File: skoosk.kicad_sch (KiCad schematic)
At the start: 90 parts, among them SW1 SW_Push, U1 ProMicro

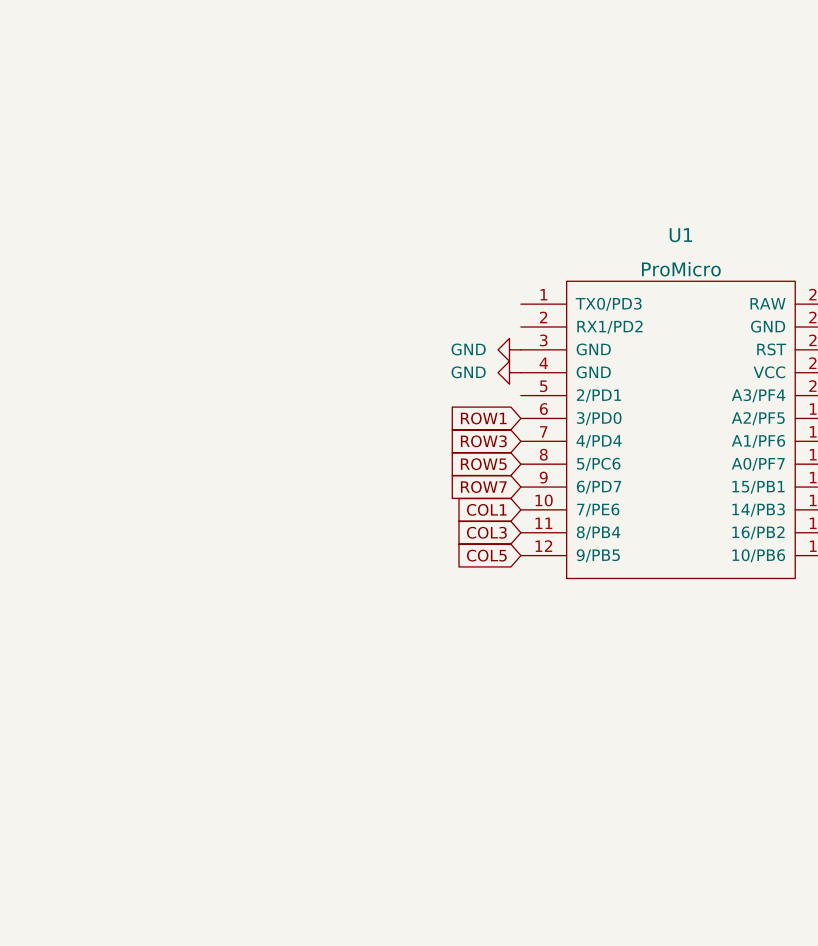
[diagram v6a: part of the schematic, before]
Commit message: GND filling done, added some ideas
maybe a rotary encoder and rgd leds?
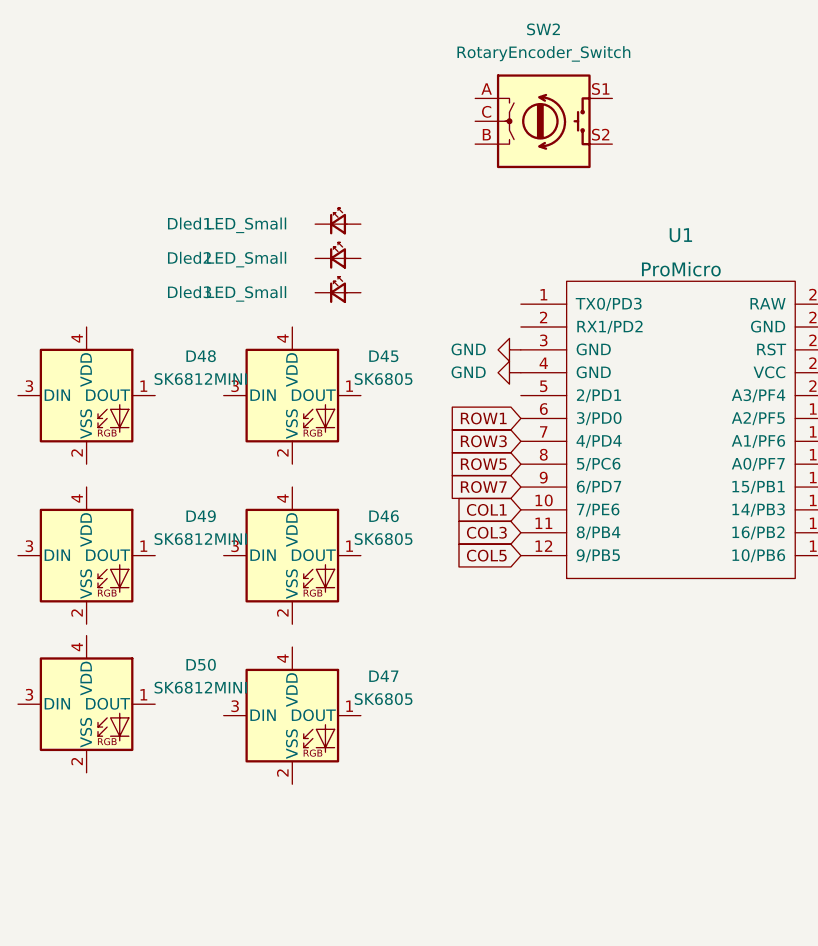
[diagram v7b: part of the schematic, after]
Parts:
- added D45, D46, D47: SK6805, LED_SMD:LED_SK6805_PLCC4_2.4x2.7mm_P1.3mm, symbol LED:SK6805
- added D48, D49, D50: SK6812MINI, LED_SMD:LED_SK6812MINI_PLCC4_3.5x3.5mm_P1.75mm, symbol LED:SK6812MINI
- added Dled1, Dled2, Dled3: LED_Small, LED_THT:LED_D5.0mm_Clear, symbol Device:LED_Small
- added SW2: RotaryEncoder_Switch, Keebio-Parts:RotaryEncoder_Alps_EC11E-Switch_Vertical_H20mm, symbol Device:RotaryEncoder_Switch
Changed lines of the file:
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@@
     (pin "2")
+  )
+  (symbol (lib_id "LED:SK6812MINI") (at -2.54 78.74 0) (unit 1)
+    (in_bom yes) (on_board yes) (fields_autoplaced)
+    (property "Reference" "D48" (id 0) (at 10.16 74.4093 0))
+    (property "Value" "SK6812MINI" (id 1) (at 10.16 76.9493 0))
+    (property "Footprint" "LED_SMD:LED_SK6812MINI_PLCC4_3.5x3.5mm_P1.75mm" (id 2) (at -1.27 86.36 0)
+      (effects (font (size 1.27 1.27)) (justify left top) hide)
+    )
+    (property "Datasheet" "https://cdn-shop.adafruit.com/product-files/2686/SK6812MINI_REV.01-1-2.pdf" (id 3) (at 0 88.265 0)
+      (effects (font (size 1.27 1.27)) (justify left top) hide)
+    )
+    (pin "1")
+    (pin "2")
+    (pin "3")
+    (pin "4")
   )
   (symbol (lib_id "MX_Alps_Hybrid:MX-NoLED") (at 154.94 92.71 0) (unit 1)
@@
     (pin "2")
   )
+  (symbol (lib_id "Device:LED_Small") (at 25.4 63.5 0) (unit 1)
+    (in_bom yes) (on_board yes)
+    (property "Reference" "Dled2" (id 0) (at 8.89 63.5 0))
+    (property "Value" "LED_Small" (id 1) (at 15.24 63.5 0))
+    (property "Footprint" "LED_THT:LED_D5.0mm_Clear" (id 2) (at 25.4 63.5 90)
+      (effects (font (size 1.27 1.27)) hide)
+    )
+    (property "Datasheet" "~" (id 3) (at 25.4 63.5 90)
+      (effects (font (size 1.27 1.27)) hide)
+    )
+    (pin "1")
+    (pin "2")
+  )
   (symbol (lib_id "MX_Alps_Hybrid:MX-NoLED") (at 256.54 74.93 0) (unit 1)
     (in_bom yes) (on_board yes) (fields_autoplaced)
@@
     (pin "2")
   )
+  (symbol (lib_id "LED:SK6805") (at 20.32 114.3 0) (unit 1)
+    (in_bom yes) (on_board yes) (fields_autoplaced)
+    (property "Reference" "D47" (id 0) (at 30.48 109.9693 0))
+    (property "Value" "SK6805" (id 1) (at 30.48 112.5093 0))
+    (property "Footprint" "LED_SMD:LED_SK6805_PLCC4_2.4x2.7mm_P1.3mm" (id 2) (at 21.59 121.92 0)
+      (effects (font (size 1.27 1.27)) (justify left top) hide)
+    )
+    (property "Datasheet" "https://cdn-shop.adafruit.com/product-files/3484/3484_Datasheet.pdf" (id 3) (at 22.86 123.825 0)
+      (effects (font (size 1.27 1.27)) (justify left top) hide)
+    )
+    (pin "1")
+    (pin "2")
+    (pin "3")
+    (pin "4")
+  )
   (symbol (lib_id "Device:D_Small") (at 204.47 81.28 90) (unit 1)
     (in_bom yes) (on_board yes) (fields_autoplaced)
@@
     (pin "2")
   )
+  (symbol (lib_id "LED:SK6805") (at 20.32 96.52 0) (unit 1)
+    (in_bom yes) (on_board yes) (fields_autoplaced)
+    (property "Reference" "D46" (id 0) (at 30.48 92.1893 0))
+    (property "Value" "SK6805" (id 1) (at 30.48 94.7293 0))
+    (property "Footprint" "LED_SMD:LED_SK6805_PLCC4_2.4x2.7mm_P1.3mm" (id 2) (at 21.59 104.14 0)
+      (effects (font (size 1.27 1.27)) (justify left top) hide)
+    )
+    (property "Datasheet" "https://cdn-shop.adafruit.com/product-files/3484/3484_Datasheet.pdf" (id 3) (at 22.86 106.045 0)
+      (effects (font (size 1.27 1.27)) (justify left top) hide)
+    )
+    (pin "1")
+    (pin "2")
+    (pin "3")
+    (pin "4")
+  )
+  (symbol (lib_id "Device:LED_Small") (at 25.4 59.69 0) (unit 1)
+    (in_bom yes) (on_board yes)
+    (property "Reference" "Dled1" (id 0) (at 8.89 59.69 0))
+    (property "Value" "LED_Small" (id 1) (at 15.24 59.69 0))
+    (property "Footprint" "LED_THT:LED_D5.0mm_Clear" (id 2) (at 25.4 59.69 90)
+      (effects (font (size 1.27 1.27)) hide)
+    )
+    (property "Datasheet" "~" (id 3) (at 25.4 59.69 90)
+      (effects (font (size 1.27 1.27)) hide)
+    )
+    (pin "1")
+    (pin "2")
+  )
   (symbol (lib_id "Device:D_Small") (at 128.27 99.06 90) (unit 1)
     (in_bom yes) (on_board yes) (fields_autoplaced)
@@
     (pin "1")
     (pin "2")
+  )
+  (symbol (lib_id "Device:RotaryEncoder_Switch") (at 48.26 48.26 0) (unit 1)
+    (in_bom yes) (on_board yes) (fields_autoplaced)
+    (property "Reference" "SW2" (id 0) (at 48.26 38.1 0))
+    (property "Value" "RotaryEncoder_Switch" (id 1) (at 48.26 40.64 0))
+    (property "Footprint" "Keebio-Parts:RotaryEncoder_Alps_EC11E-Switch_Vertical_H20mm" (id 2) (at 44.45 44.196 0)
+      (effects (font (size 1.27 1.27)) hide)
+    )
+    (property "Datasheet" "~" (id 3) (at 48.26 41.656 0)
+      (effects (font (size 1.27 1.27)) hide)
+    )
+    (pin "A")
+    (pin "B")
+    (pin "C")
+    (pin "S1")
+    (pin "S2")
   )
   (symbol (lib_id "Device:D_Small") (at 267.97 116.84 90) (unit 1)
@@
     (pin "2")
   )
+  (symbol (lib_id "LED:SK6812MINI") (at -2.54 113.03 0) (unit 1)
+    (in_bom yes) (on_board yes) (fields_autoplaced)
+    (property "Reference" "D50" (id 0) (at 10.16 108.6993 0))
+    (property "Value" "SK6812MINI" (id 1) (at 10.16 111.2393 0))
+    (property "Footprint" "LED_SMD:LED_SK6812MINI_PLCC4_3.5x3.5mm_P1.75mm" (id 2) (at -1.27 120.65 0)
+      (effects (font (size 1.27 1.27)) (justify left top) hide)
+    )
+    (property "Datasheet" "https://cdn-shop.adafruit.com/product-files/2686/SK6812MINI_REV.01-1-2.pdf" (id 3) (at 0 122.555 0)
+      (effects (font (size 1.27 1.27)) (justify left top) hide)
+    )
+    (pin "1")
+    (pin "2")
+    (pin "3")
+    (pin "4")
+  )
   (symbol (lib_id "MX_Alps_Hybrid:MX-NoLED") (at 269.24 110.49 0) (unit 1)
     (in_bom yes) (on_board yes) (fields_autoplaced)
@@
     (property "Datasheet" "" (id 3) (at 253.365 75.565 0)
       (effects (font (size 1.524 1.524)) hide)
+    )
+    (pin "1")
+    (pin "2")
+  )
+  (symbol (lib_id "Device:LED_Small") (at 25.4 67.31 0) (unit 1)
+    (in_bom yes) (on_board yes)
+    (property "Reference" "Dled3" (id 0) (at 8.89 67.31 0))
+    (property "Value" "LED_Small" (id 1) (at 15.24 67.31 0))
+    (property "Footprint" "LED_THT:LED_D5.0mm_Clear" (id 2) (at 25.4 67.31 90)
+      (effects (font (size 1.27 1.27)) hide)
+    )
+    (property "Datasheet" "~" (id 3) (at 25.4 67.31 90)
+      (effects (font (size 1.27 1.27)) hide)
     )
     (pin "1")
@@
     (pin "2")
   )
+  (symbol (lib_id "LED:SK6805") (at 20.32 78.74 0) (unit 1)
+    (in_bom yes) (on_board yes) (fields_autoplaced)
+    (property "Reference" "D45" (id 0) (at 30.48 74.4093 0))
+    (property "Value" "SK6805" (id 1) (at 30.48 76.9493 0))
+    (property "Footprint" "LED_SMD:LED_SK6805_PLCC4_2.4x2.7mm_P1.3mm" (id 2) (at 21.59 86.36 0)
+      (effects (font (size 1.27 1.27)) (justify left top) hide)
+    )
+    (property "Datasheet" "https://cdn-shop.adafruit.com/product-files/3484/3484_Datasheet.pdf" (id 3) (at 22.86 88.265 0)
+      (effects (font (size 1.27 1.27)) (justify left top) hide)
+    )
+    (pin "1")
+    (pin "2")
+    (pin "3")
+    (pin "4")
+  )
   (symbol (lib_id "MX_Alps_Hybrid:MX-NoLED") (at 180.34 74.93 0) (unit 1)
     (in_bom yes) (on_board yes) (fields_autoplaced)
@@
     (pin "1")
     (pin "2")
+  )
+  (symbol (lib_id "LED:SK6812MINI") (at -2.54 96.52 0) (unit 1)
+    (in_bom yes) (on_board yes) (fields_autoplaced)
+    (property "Reference" "D49" (id 0) (at 10.16 92.1893 0))
+    (property "Value" "SK6812MINI" (id 1) (at 10.16 94.7293 0))
+    (property "Footprint" "LED_SMD:LED_SK6812MINI_PLCC4_3.5x3.5mm_P1.75mm" (id 2) (at -1.27 104.14 0)
+      (effects (font (size 1.27 1.27)) (justify left top) hide)
+    )
+    (property "Datasheet" "https://cdn-shop.adafruit.com/product-files/2686/SK6812MINI_REV.01-1-2.pdf" (id 3) (at 0 106.045 0)
+      (effects (font (size 1.27 1.27)) (justify left top) hide)
+    )
+    (pin "1")
+    (pin "2")
+    (pin "3")
+    (pin "4")
   )
   (symbol (lib_id "MX_Alps_Hybrid:MX-NoLED") (at 167.64 129.54 0) (unit 1)
@@
       (reference "D44") (unit 1) (value "D_Small") (footprint "Diode_THT:D_DO-35_SOD27_P7.62mm_Horizontal")
     )
+    (path "/f2269e17-06e4-4bc5-b70d-2e821d0be1bd"
+      (reference "D45") (unit 1) (value "SK6805") (footprint "LED_SMD:LED_SK6805_PLCC4_2.4x2.7mm_P1.3mm")
+    )
+    (path "/80657436-7690-4ec7-a75c-796ec75e39c3"
+      (reference "D46") (unit 1) (value "SK6805") (footprint "LED_SMD:LED_SK6805_PLCC4_2.4x2.7mm_P1.3mm")
+    )
+    (path "/4b353165-f2c3-49f2-9e42-58fa88847caa"
+      (reference "D47") (unit 1) (value "SK6805") (footprint "LED_SMD:LED_SK6805_PLCC4_2.4x2.7mm_P1.3mm")
+    )
+    (path "/0405a70f-1556-45d0-b5d0-00982c25e7a7"
+      (reference "D48") (unit 1) (value "SK6812MINI") (footprint "LED_SMD:LED_SK6812MINI_PLCC4_3.5x3.5mm_P1.75mm")
+    )
+    (path "/fb41683d-d992-4479-8b0f-8ca2ea4dd9ad"
+      (reference "D49") (unit 1) (value "SK6812MINI") (footprint "LED_SMD:LED_SK6812MINI_PLCC4_3.5x3.5mm_P1.75mm")
+    )
+    (path "/d29fc9cf-50db-4310-9d2d-7ff4bcef9d11"
+      (reference "D50") (unit 1) (value "SK6812MINI") (footprint "LED_SMD:LED_SK6812MINI_PLCC4_3.5x3.5mm_P1.75mm")
+    )
+    (path "/8c6ba95d-bc71-48e4-a6e9-5e9b2165cc31"
+      (reference "Dled1") (unit 1) (value "LED_Small") (footprint "LED_THT:LED_D5.0mm_Clear")
+    )
+    (path "/357288e2-3bab-4656-8194-a467f939e737"
+      (reference "Dled2") (unit 1) (value "LED_Small") (footprint "LED_THT:LED_D5.0mm_Clear")
+    )
+    (path "/db97c10f-a3f4-4602-b20b-97f54a0e53c4"
+      (reference "Dled3") (unit 1) (value "LED_Small") (footprint "LED_THT:LED_D5.0mm_Clear")
+    )
     (path "/06d6f48f-e469-4354-9f3f-73c3c7e47130"
       (reference "MX1") (unit 1) (value "MX-NoLED") (footprint "MX_Only:MXOnly-1.25U-NoLED")
@@
       (reference "SW1") (unit 1) (value "SW_Push") (footprint "random-keyboard-parts:SKQG-1155865")
     )
+    (path "/a32d9a48-589d-4751-83ef-4edfc0327379"
+      (reference "SW2") (unit 1) (value "RotaryEncoder_Switch") (footprint "Keebio-Parts:RotaryEncoder_Alps_EC11E-Switch_Vertical_H20mm")
+    )
     (path "/b1d8b9c1-d0cf-460d-9610-64eb34437dc3"

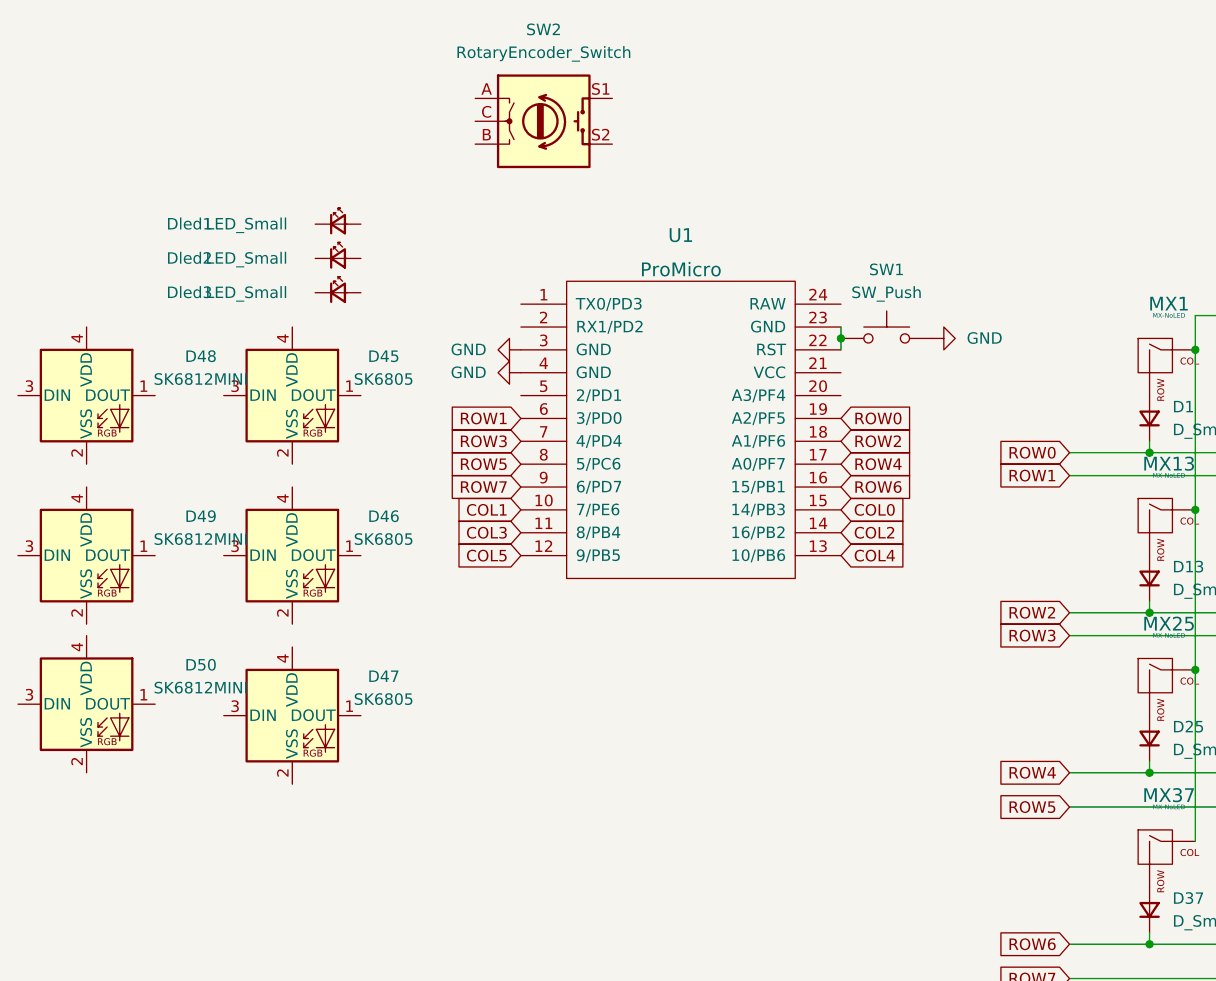
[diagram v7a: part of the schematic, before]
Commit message: ordering schematics to add rotary and rgd
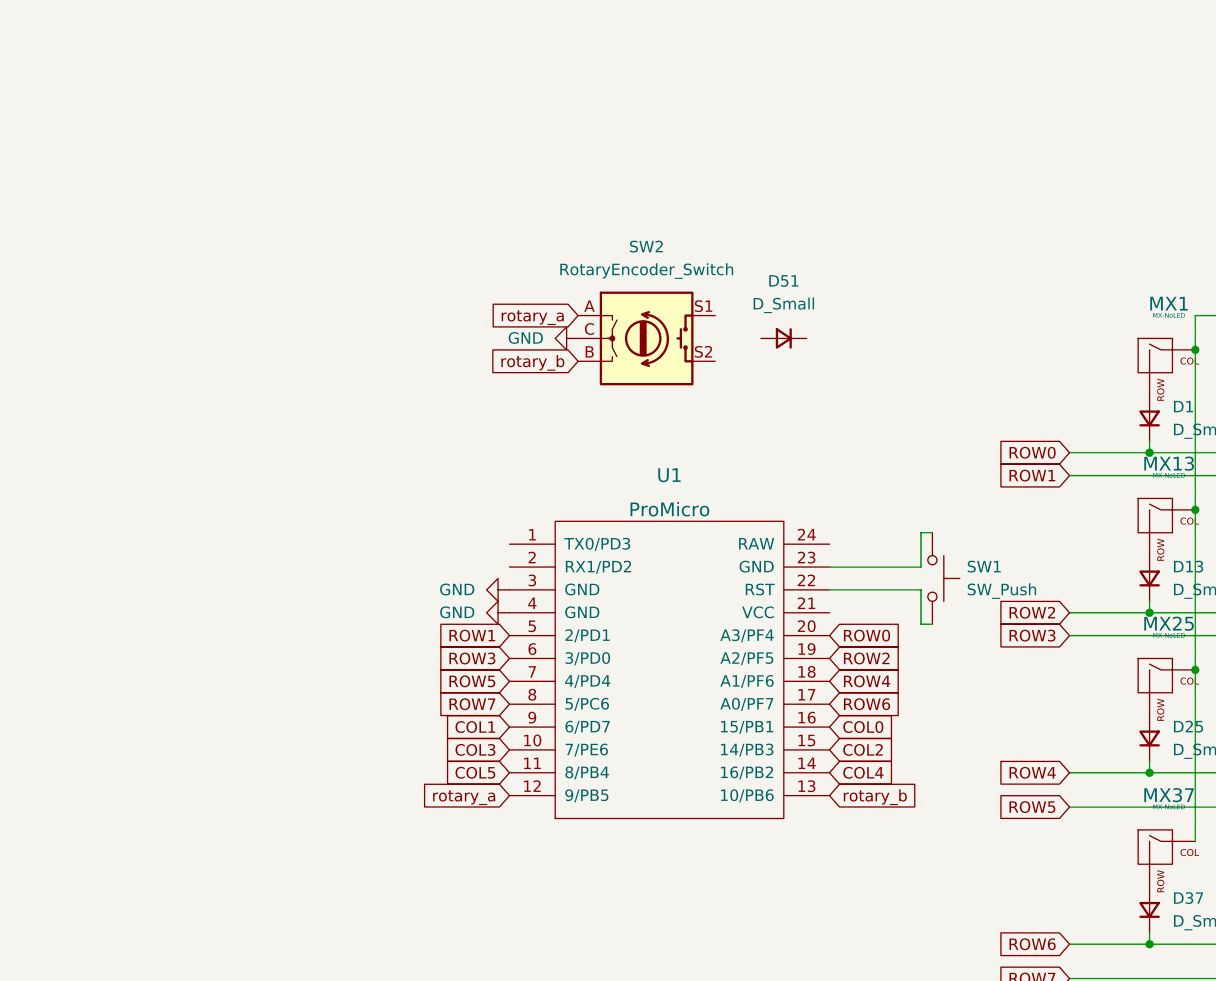
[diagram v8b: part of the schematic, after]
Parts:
- removed D45, D46, D47: SK6805, LED_SMD:LED_SK6805_PLCC4_2.4x2.7mm_P1.3mm, symbol LED:SK6805
- removed D48, D49, D50: SK6812MINI, LED_SMD:LED_SK6812MINI_PLCC4_3.5x3.5mm_P1.75mm, symbol LED:SK6812MINI
- removed Dled1, Dled2, Dled3: LED_Small, LED_THT:LED_D5.0mm_Clear, symbol Device:LED_Small
- added D51: D_Small, symbol Device:D_Small
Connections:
- net COL0: now also U1.16 (15/PB1); no longer U1.15 (14/PB3)
- net COL1: now also U1.9 (6/PD7); no longer U1.10 (7/PE6)
- net COL2: now also U1.15 (14/PB3); no longer U1.14 (16/PB2)
- net COL3: now also U1.10 (7/PE6); no longer U1.11 (8/PB4)
- net COL4: now also U1.14 (16/PB2); no longer U1.13 (10/PB6)
- net COL5: now also U1.11 (8/PB4); no longer U1.12 (9/PB5)
- net GND: now also SW2.C; no longer SW1.2
- net ROW0: now also U1.20 (A3/PF4); no longer U1.19 (A2/PF5)
- net ROW1: now also U1.5 (2/PD1); no longer U1.6 (3/PD0)
- net ROW2: now also U1.19 (A2/PF5); no longer U1.18 (A1/PF6)
- net ROW3: now also U1.6 (3/PD0); no longer U1.7 (4/PD4)
- net ROW4: now also U1.18 (A1/PF6); no longer U1.17 (A0/PF7)
- net ROW5: now also U1.7 (4/PD4); no longer U1.8 (5/PC6)
- net ROW6: now also U1.17 (A0/PF7); no longer U1.16 (15/PB1)
- net ROW7: now also U1.8 (5/PC6); no longer U1.9 (6/PD7)
- net at SW1.1, U1.23 (GND): no longer U1.22 (RST)
- net rotary_a: now reaches SW2.A
- net rotary_a: now also U1.12 (9/PB5)
- net rotary_b: now reaches SW2.B
- net rotary_b: now also U1.13 (10/PB6)
- new net: SW1.2, U1.22 (RST)
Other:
- moved on the sheet: SW1, SW2, U1
